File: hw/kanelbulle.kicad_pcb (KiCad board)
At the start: 2 copper layers, 82.4 x 88.4 mm, 76 parts, among them J1 USB, U1 LPC1114/302, U2 PCA9685, U3 ULN2003A, U4 ULN2003A, U5 ULN2003A

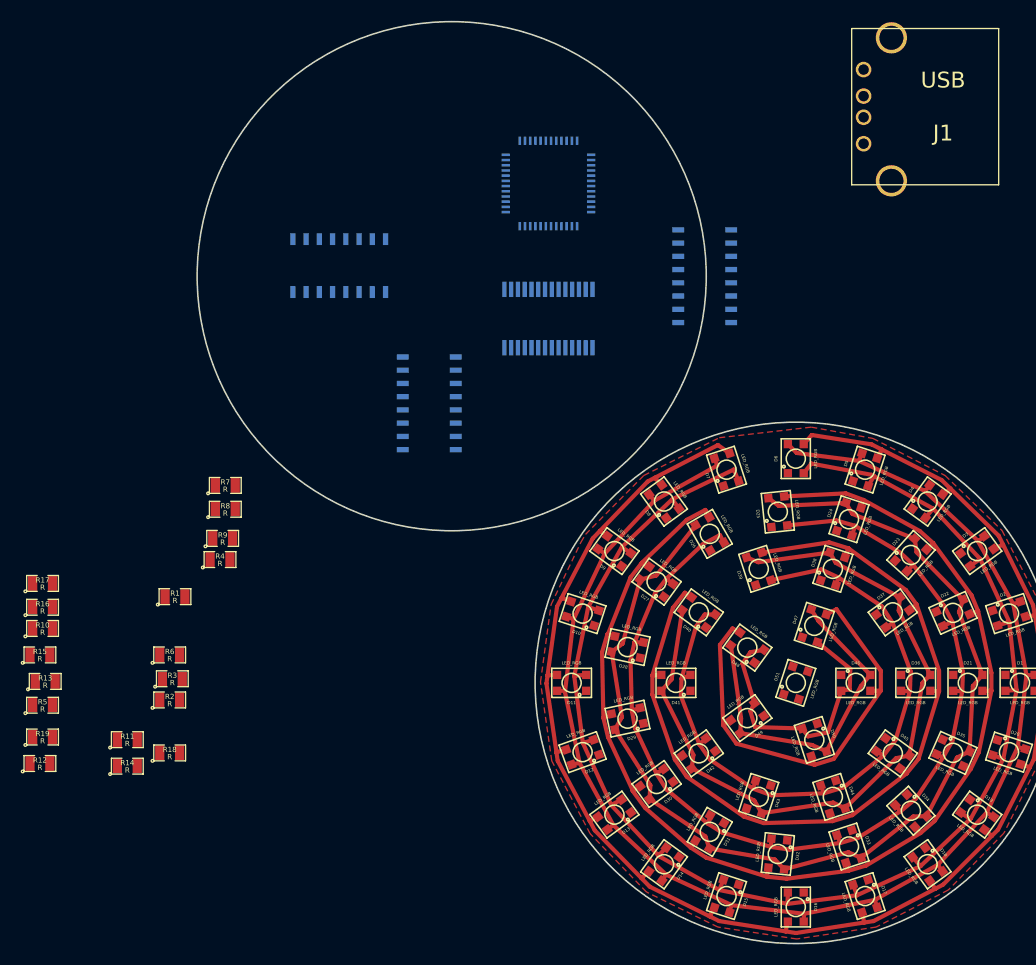
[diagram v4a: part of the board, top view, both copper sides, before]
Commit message: connected some OC drivers
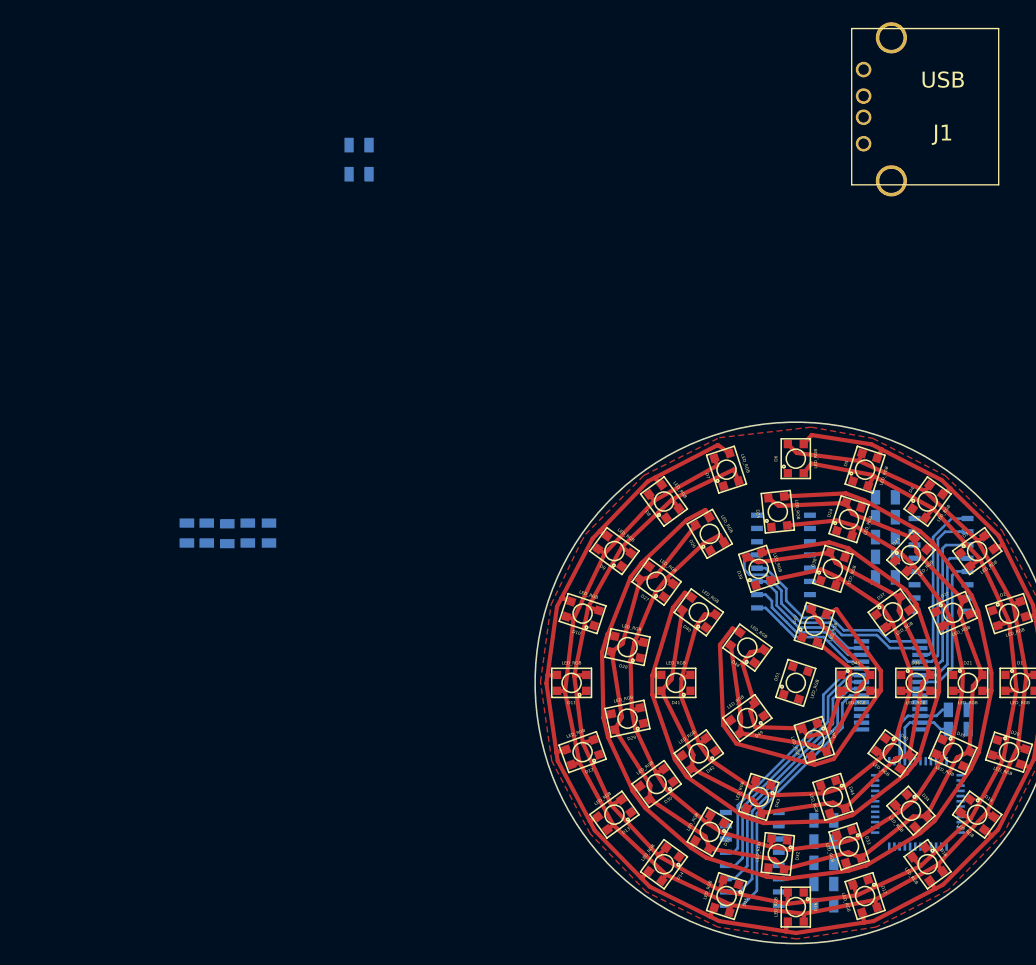
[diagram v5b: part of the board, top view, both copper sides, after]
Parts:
- R1, R10, R11, R12, R13, R14, R15, R16, R17, R18, R19, R2, R3, R4, R5, R6, R7, R8, R9: moved to B.Cu
- moved R15 82.5 mm to (208.6, 132.2), turned to 180 degrees
- moved R19 82.3 mm to (208.6, 139.9), turned to 180 degrees
- moved R16 81.3 mm to (208.6, 134.1), turned to 180 degrees
- moved R17 81.0 mm to (208.6, 136.0), turned to 180 degrees
- moved R5 77.3 mm to (202.7, 171.3)
- moved R3 75.5 mm to (215.6, 154.4), turned to 180 degrees
- moved R4 72.3 mm to (215.6, 152.6), turned to 180 degrees
- moved R18 71.2 mm to (208.6, 137.9), turned to 180 degrees
- moved U3 69.3 mm to (195.8, 166.9), turned to 90 degrees
- moved U1 69.3 mm to (211.7, 161.6)
- moved R7 67.9 mm to (202.7, 167.3)
- moved R6 66.5 mm to (202.7, 169.3)
- moved R8 65.7 mm to (202.7, 165.2)
- moved R9 63.7 mm to (202.7, 163.2)
- moved R2 53.6 mm to (158.1, 101.2)
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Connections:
- net N-000008 renamed /RST
- net N-000009 renamed /ISP
- U1 pad 15: (no net) -> /SCL
- U1 pad 16: (no net) -> /SDA
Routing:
- net N-0000062: track 0.00 -> 27.1 mm
- net N-0000063: track 0.00 -> 26.3 mm
- net N-000001: track 0.00 -> 25.4 mm
- net N-000002: track 0.00 -> 24.8 mm
- net N-000003: track 0.00 -> 24.1 mm
- net N-0000050: track 0.00 -> 23.1 mm
- net N-0000049: track 0.00 -> 19.2 mm
- net N-0000056: track 0.00 -> 16.3 mm
- net N-0000057: track 0.00 -> 16.3 mm
- net N-0000058: track 0.00 -> 15.9 mm
- net N-0000016: track 0.00 -> 15.0 mm
- net N-0000017: track 0.00 -> 14.2 mm
- net N-0000048: track 0.00 -> 13.4 mm
- net N-0000047: track 0.00 -> 12.8 mm
- net N-0000046: track 0.00 -> 12.2 mm
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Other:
- board size 82.4 x 88.4 mm -> 50 x 50 mm

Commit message: decoupling
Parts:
- added C1: C, SM1206, F.Cu at (228.0, 166.1)
- added C2: C, SM1206, F.Cu at (227.5, 169.9)
- added C3: C, SM0805, F.Cu at (234.0, 172.5)
- added C4: C, SM0805, F.Cu at (235.0, 174.6)
- added C5: C, SM0805, F.Cu at (235.5, 176.5)
- added C6: C, SM0805, F.Cu at (235.3, 178.6)
- added C7: C, SM0805, F.Cu at (233.9, 170.2)

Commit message: 3d renders
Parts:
- moved J1 171.8 mm to (56.6, 178.8)
- moved C2 151.9 mm to (91.2, 237.0)
- moved C3 151.8 mm to (87.7, 213.1)
- moved C5 151.8 mm to (89.2, 217.2)
- moved C7 151.8 mm to (87.6, 210.9)
- moved C4 151.8 mm to (88.7, 215.2)
- moved C6 151.8 mm to (89.0, 219.3)
- moved C1 150.2 mm to (92.5, 230.9)
- moved R1 115.2 mm to (90.8, 191.9)
- moved R2 115.2 mm to (90.8, 194.7)
- moved R10 95.9 mm to (78.1, 199.6)
- moved R11 95.9 mm to (76.1, 199.6)
- moved R12 95.9 mm to (74.1, 199.7)
- moved R13 95.9 mm to (72.1, 199.6)
- moved R14 95.9 mm to (70.2, 199.6)
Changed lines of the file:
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@@
     (links 265)
     (no_connects 58)
-    (area 174.924999 124.924999 225.075001 175.075001)
+    (area 55.232299 117.925001 225.075001 238.455201)
     (thickness 1.6)
     (drawings 3)
@@
     (visible_elements FFFFFFFF)
     (pcbplotparams
-      (layerselection 3178497)
-      (usegerberextensions true)
+      (layerselection 1)
+      (usegerberextensions false)
       (excludeedgelayer true)
       (linewidth 0.150000)
@@
       (padsonsilk false)
       (subtractmaskfromsilk false)
-      (outputformat 1)
+      (outputformat 2)
       (mirror false)
-      (drillshape 1)
+      (drillshape 0)
       (scaleselection 1)
       (outputdirectory ""))
@@
   )
   (module USB_A (layer F.Cu)
-    (at 206.502 94.742)
+    (at 56.642 178.816)
     (fp_text reference J1 (at 7.62 2.54) (layer F.SilkS)
       (effects (font (size 1.524 1.524) (thickness 0.3048)))
@@
   )
   (module SM0805 (layer B.Cu)
-    (at 158.115 101.219)
+    (at 90.805 194.691)
     (attr smd)
     (fp_text reference R2 (at 0 0.3175) (layer B.SilkS)
@@
   )
   (module SM0805 (layer B.Cu)
-    (at 158.115 98.425)
+    (at 90.805 191.897)
     (attr smd)
     (fp_text reference R1 (at 0 0.3175) (layer B.SilkS)
@@
   )
   (module SM0805 (layer B.Cu)
-    (at 149.479 135.636 90)
+    (at 78.105 199.644 90)
     (attr smd)
     (fp_text reference R10 (at 0 0.3175 90) (layer B.SilkS)
@@
   )
   (module SM0805 (layer B.Cu)
-    (at 147.447 135.636 90)
+    (at 76.073 199.644 90)
     (attr smd)
     (fp_text reference R11 (at 0 0.3175 90) (layer B.SilkS)
@@
   )
   (module SM0805 (layer B.Cu)
-    (at 145.4785 135.6995 90)
+    (at 74.1045 199.7075 90)
     (attr smd)
     (fp_text reference R12 (at 0 0.3175 90) (layer B.SilkS)
@@
   )
   (module SM0805 (layer B.Cu)
-    (at 143.51 135.636 90)
+    (at 72.136 199.644 90)
     (attr smd)
     (fp_text reference R13 (at 0 0.3175 90) (layer B.SilkS)
@@
   )
   (module SM0805 (layer B.Cu)
-    (at 141.605 135.636 90)
+    (at 70.231 199.644 90)
     (attr smd)
     (fp_text reference R14 (at 0 0.3175 90) (layer B.SilkS)
@@
   )
   (module SM1206 (layer F.Cu)
-    (at 227.457 169.926)
+    (at 91.186 236.982)
     (attr smd)
     (fp_text reference C2 (at 0 0) (layer F.SilkS)
@@
   )
   (module SM1206 (layer F.Cu)
-    (at 228.0285 166.116)
+    (at 92.456 230.886)
     (attr smd)
     (fp_text reference C1 (at 0 0) (layer F.SilkS)
@@
   )
   (module SM0805 (layer F.Cu)
-    (at 233.9975 172.466)
+    (at 87.6935 213.106)
     (attr smd)
     (fp_text reference C3 (at 0 -0.3175) (layer F.SilkS)
@@
   )
   (module SM0805 (layer F.Cu)
-    (at 235.0135 174.5615)
+    (at 88.7095 215.2015)
     (attr smd)
     (fp_text reference C4 (at 0 -0.3175) (layer F.SilkS)
@@
   )
   (module SM0805 (layer F.Cu)
-    (at 235.458 176.53)
+    (at 89.154 217.17)
     (attr smd)
     (fp_text reference C5 (at 0 -0.3175) (layer F.SilkS)
@@
   )
   (module SM0805 (layer F.Cu)
-    (at 235.331 178.6255)
+    (at 89.027 219.2655)
     (attr smd)
     (fp_text reference C6 (at 0 -0.3175) (layer F.SilkS)
@@
   )
   (module SM0805 (layer F.Cu)
-    (at 233.934 170.2435)
+    (at 87.63 210.8835)
     (attr smd)
     (fp_text reference C7 (at 0 -0.3175) (layer F.SilkS)

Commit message: aaawww yeeeeaaaahhhh
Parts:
- removed J1: USB, USB_A
- added C8: C, SM1206, B.Cu at (192.8, 150.1)
- added P1: USB, USB_FULHAKK, B.Cu at (195.6, 146.6)
- added P2: CONN_6, SMD_ARRAY-6X1, B.Cu at (220.7, 150.1)
- added U6: NCP1117ST33T3G, DPAK2, B.Cu at (189.5, 149.9)
- C1, C2, C3, C4, C5, C6, C7: moved to B.Cu
- moved C7 148.9 mm to (218.9, 140.6), turned to 180 degrees
- moved C6 139.5 mm to (206.2, 143.6), turned to 270 degrees
- moved R14 139.0 mm to (194.2, 136.7), turned to 0 degrees
- moved R13 136.5 mm to (194.2, 138.6), turned to 0 degrees
- moved R11 135.5 mm to (193.4, 131.8), turned to 0 degrees
- moved R10 134.7 mm to (193.4, 130.0), turned to 0 degrees
- moved R1 133.3 mm to (217.6, 150.7)
- moved R2 132.9 mm to (218.1, 156.2)
- moved C3 132.7 mm to (207.4, 155.8)
- moved R12 131.3 mm to (191.4, 140.7), turned to 270 degrees
- moved C1 123.6 mm to (181.6, 145.3)
- moved C5 122.8 mm to (182.1, 136.9), turned to 90 degrees
- moved C2 121.7 mm to (183.8, 158.0)
- moved C4 110.0 mm to (184.0, 160.3)
- moved U4 12.3 mm to (186.6, 137.9)
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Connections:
- U1 pad 14: (no net) -> /LEDOE
- U1 pad 41: N-0000040 -> GND
- U1 pad 46: (no net) -> /RX
- U1 pad 47: (no net) -> /TX
- U1 pad 5: N-0000040 -> GND
- U2 pad 1: (no net) -> 3V3
- U2 pad 2: (no net) -> GND
- U2 pad 23: (no net) -> /LEDOE
- U2 pad 24: (no net) -> GND
- U2 pad 3: (no net) -> 3V3
- U2 pad 4: (no net) -> GND
- U2 pad 5: (no net) -> 3V3
- U3 pad 6: (no net) -> GND
- U3 pad 7: (no net) -> GND
- U4 pad 6: (no net) -> GND
- U4 pad 7: (no net) -> GND
- U5 pad 6: (no net) -> GND
- U5 pad 7: (no net) -> GND
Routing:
- net 3V3: track 0.00 -> 73.4 mm, vias 0 -> 12
- net N-0000054: track 19.2 -> 51.4 mm
- net N-0000057: track 23.1 -> 52.9 mm
- net /RX: track 0.00 -> 29.4 mm
- net /TX: track 0.00 -> 26.6 mm
- net /RST: track 0.00 -> 24.6 mm
- net /ISP: track 0.00 -> 22.5 mm
- net N-0000058: track 13.4 -> 35.8 mm
- net N-0000059: track 12.8 -> 34.9 mm
- net N-0000033: track 12.2 -> 33.7 mm
- net N-0000014: track 0.00 -> 19.1 mm
- net /R5: track 0.00 -> 16.7 mm, vias 0 -> 1
- net N-0000023: track 27.1 -> 10.6 mm
- net N-0000015: track 0.00 -> 16.4 mm
- net /G5: track 0.00 -> 15.3 mm, vias 0 -> 1
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- added copper zone on B.Cu, net GND
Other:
- net class power added: clearance 0.2032, trace_width 0.4, via_dia 0.95, via_drill 0.75
